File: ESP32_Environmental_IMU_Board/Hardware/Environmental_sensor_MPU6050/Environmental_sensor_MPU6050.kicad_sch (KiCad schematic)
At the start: 55 parts, among them J1 Conn_01x04_Pin, J2 Conn_01x04_Pin, J3 USB_C_Receptacle_USB2.0_16P, J4 Micro_SD_Card, SW1 SW_Push, SW2 SW_Push, U2 AP2112K-3.3, U3 USBLC6-2P6, U4 ESP32-S3-WROOM-1, U5 BME280, U6 DS3231M

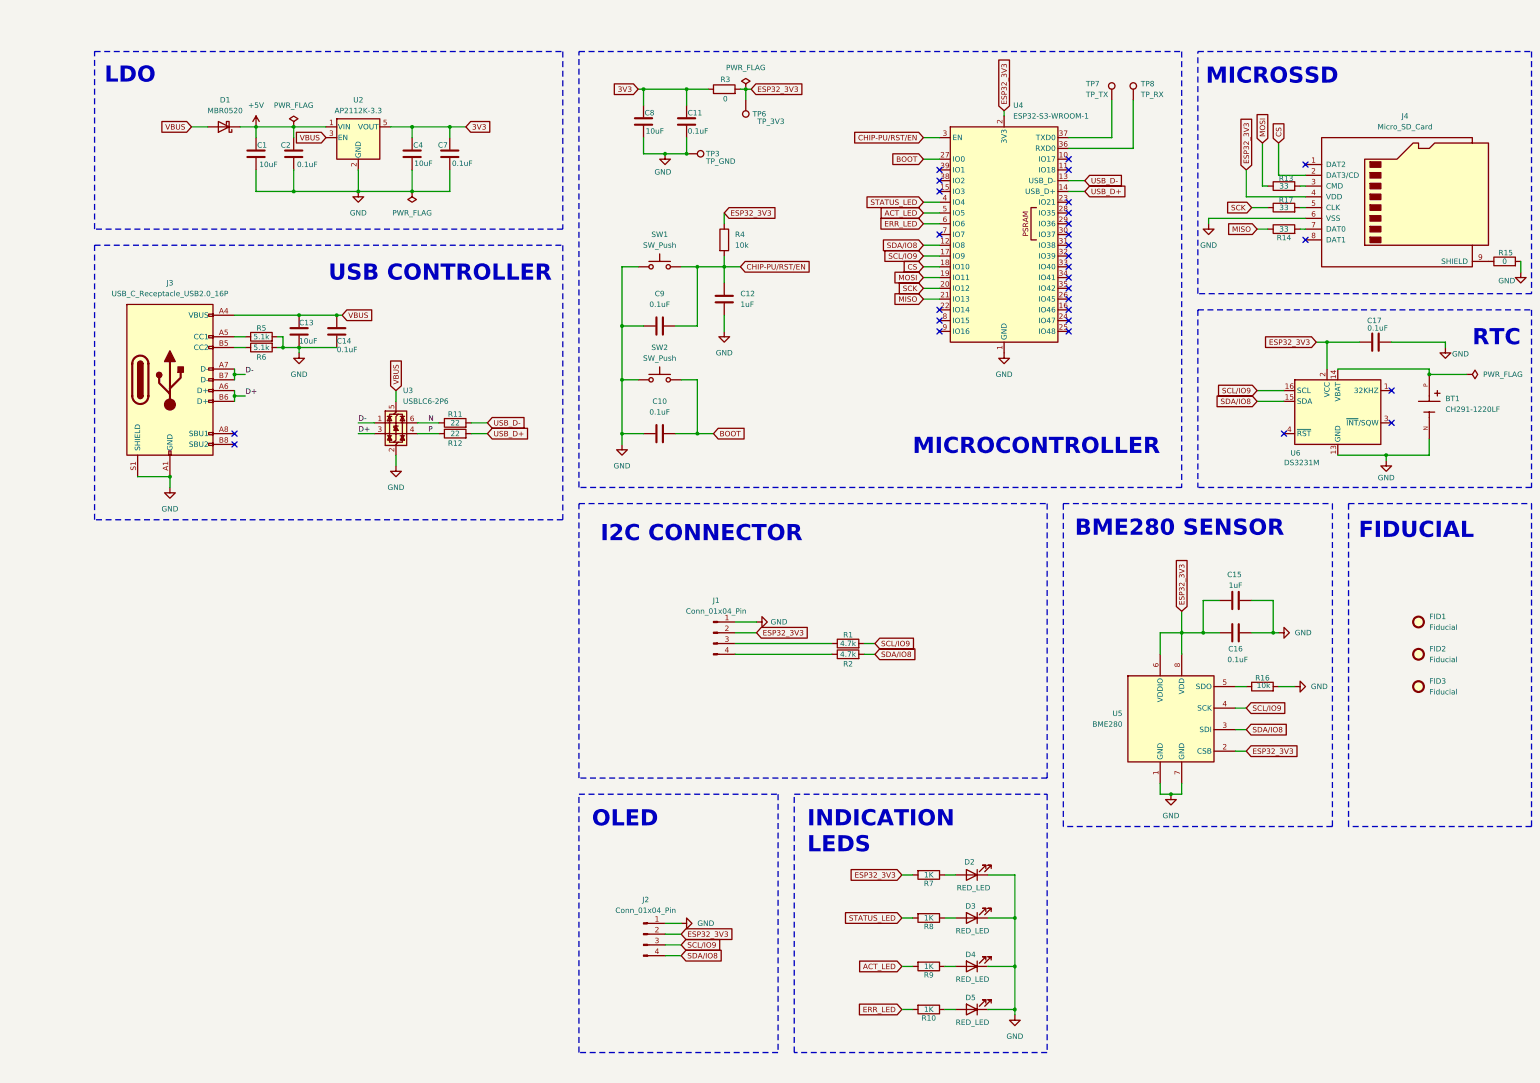
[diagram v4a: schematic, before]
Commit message: Charging moduke and buck converter added
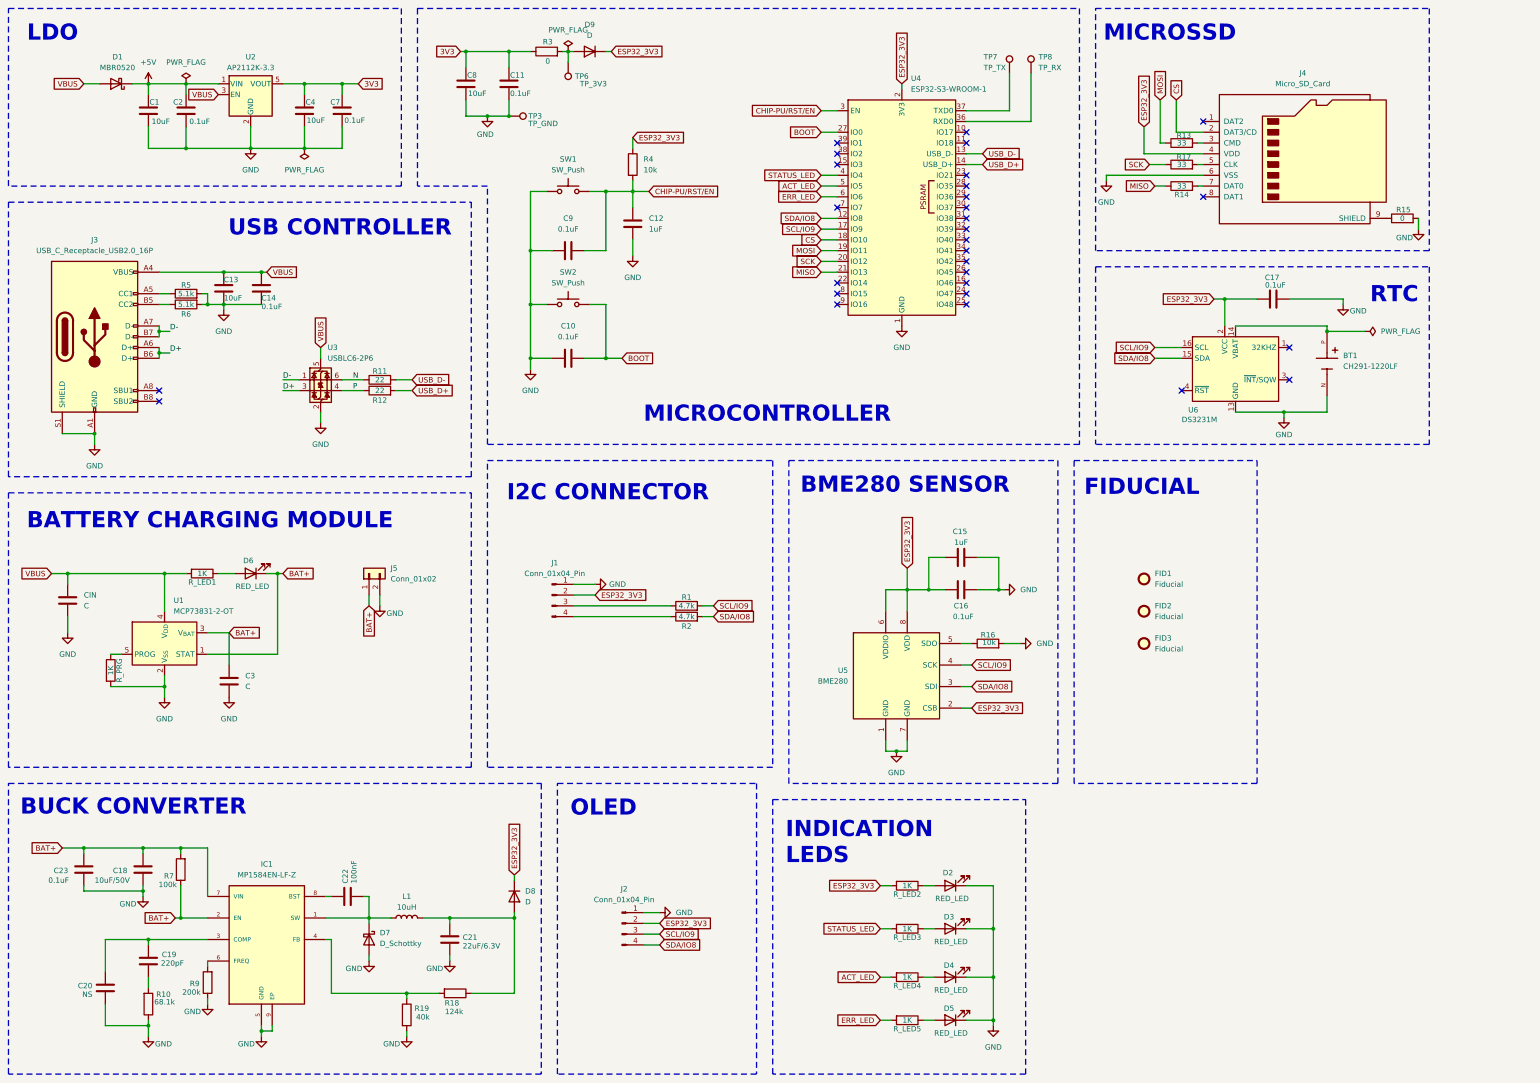
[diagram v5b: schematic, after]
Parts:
- added C18: 10uF/50V, Capacitor_SMD:C_0805_2012Metric, symbol Device:C
- added C19: 220pF, Capacitor_SMD:C_0805_2012Metric, symbol Device:C
- added C20: NS, Capacitor_SMD:C_0805_2012Metric, symbol Device:C
- added C21: 22uF/6.3V, Capacitor_SMD:C_0805_2012Metric, symbol Device:C
- added C22: 100nF, Capacitor_SMD:C_0805_2012Metric, symbol Device:C
- added C23: 0.1uF, Capacitor_SMD:C_0805_2012Metric, symbol Device:C
- added C3, CIN: C, symbol Device:C
- added D6: RED_LED, LED_SMD:LED_0201_0603Metric, symbol Device:LED
- added D7: D_Schottky, symbol Device:D_Schottky
- added D8, D9: D, symbol Device:D
- added IC1: MP1584EN-LF-Z, MP1584EN-LF-Z:SOIC127P600X170-9N, symbol MP1584EN-LF-Z:MP1584EN-LF-Z
- added J5: Conn_01x02, symbol Connector_Generic:Conn_01x02
- added L1: 10uH, symbol Device:L
- added R10: 68.1k, Resistor_SMD:R_0603_1608Metric, symbol Device:R
- added R18: 124k, Resistor_SMD:R_0603_1608Metric, symbol Device:R
- added R19: 40k, Resistor_SMD:R_0603_1608Metric, symbol Device:R
- added R7: 100k, Resistor_SMD:R_0603_1608Metric, symbol Device:R
- added R9: 200k, Resistor_SMD:R_0603_1608Metric, symbol Device:R
- added R_LED1, R_PRG: 1K, Resistor_SMD:R_0603_1608Metric, symbol Device:R
- added U1: MCP73831-2-OT, Package_TO_SOT_SMD:SOT-23-5, symbol Battery_Management:MCP73831-2-OT
- renumbered R7 to R_LED2, R8 to R_LED3, R9 to R_LED4, R10 to R_LED5
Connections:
- net ESP32_3V3: now also D8.1 (K), D9.1 (K); no longer R3.2, TP6.1
- net GND: now also C18.2, C20.2, C21.2, C23.2, C3.2, CIN.1, D7.2 (A), IC1.5 (GND), IC1.9 (EP), J5.2 (Pin_2), R10.1, R19.2, R9.1, R_PRG.2, U1.2 (V_{SS})
- net VBUS: now also CIN.2, R_LED1.2, U1.4 (V_{DD})
- new net: C22.2, D7.1 (K), IC1.1 (SW), L1.1
- new net: C19.1, C20.1, IC1.3 (COMP)
- new net: IC1.4 (FB), R18.2, R19.1
- new net: IC1.6 (FREQ), R9.2
- new net: C22.1, IC1.8 (BST)
- new net: C21.1, D8.2 (A), L1.2, R18.1
- new net: D9.2 (A), R3.2, TP6.1
- new net: C19.2, R10.2
- new net: D6.2 (A), R_LED1.1
- new net: R_PRG.1, U1.5 (PROG)
- new net BAT+: C18.1, C23.1, C3.1, D6.1 (K), IC1.2 (EN), IC1.7 (VIN), J5.1 (Pin_1), R7.1, R7.2, U1.1 (STAT), U1.3 (V_{BAT})
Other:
- note added: "BATTERY CHARGING MODULE"
- note added: "BUCK CONVERTER"
- moved on the sheet: BT1, C1, C10, C11, C12, C13, C14, C15, C16, C17, C2, C4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

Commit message: Sensor Architecture improvised in the Schematics
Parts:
- removed R1, R2: 4.7k, Resistor_SMD:R_0603_1608Metric, symbol Device:R
- added C22, C23: 100nF, Capacitor_SMD:C_0805_2012Metric, symbol Device:C
- added C24: 1uF, Capacitor_SMD:C_0603_1608Metric, symbol Device:C
- added C25: 0.1uF, Capacitor_SMD:C_0603_1608Metric, symbol Device:C
- added R12, R13: 4.7k, Resistor_SMD:R_0603_1608Metric, symbol Device:R
- added U10: MLX90614ESF-BAA-000-TU, MLX90614ESF-BAA-000-TU:TO254P942H425-4, symbol MLX90614ESF-BAA-000-TU:MLX90614ESF-BAA-000-TU
- added U6: SCD40-D-R2, Sensor:Sensirion_SCD4x-1EP_10.1x10.1mm_P1.25mm_EP4.8x4.8mm, symbol Sensor_Gas:SCD40-D-R2
- added U8: ENS160-BGLM, ENS160-BGLM:XDCR_ENS160-BGLM, symbol ENS160-BGLM:ENS160-BGLM
- added U9: OPT3001IDNPRQ1, OPT3001IDNPRQ1:SON65P200X200X65-7N, symbol OPT3001IDNPRQ1:OPT3001IDNPRQ1
- renumbered C23 to C1, C4 to C10, C7 to C11, C22 to C12, C21 to C13, C8 to C14, C11 to C15, C9 to C16, C10 to C17, C12 to C18, C15 to C19, C20 to C2, C16 to C20, C17 to C21, C18 to C3, C1 to C4, C19 to C5, C2 to C6, C13 to C7, C3 to C8, C14 to C9, CIN to CIN1, D6 to D2, D7 to D3, D8 to D4, D9 to D5, D2 to D6, D3 to D7, D4 to D8, D5 to D9, J3 to J1, J5 to J2, J2 to J3, J1 to J4, J4 to J5, R10 to R1, R3 to R10, R4 to R11, R16 to R14, R13 to R15, R17 to R16, R14 to R17, R15 to R18, R7 to R2, R5 to R3, R6 to R4, R9 to R5, R11 to R6, R12 to R7, R19 to R8, R18 to R9, R_PRG to R_PRG1, TP3 to TP1, TP6 to TP2, TP7 to TP3, TP8 to TP4, U5 to U4, U4 to U5, U6 to U7
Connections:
- net BAT+: no longer D2.1 (K), U1.1 (STAT)
- net ESP32_3V3: now also C22.1, C23.1, C24.1, C25.1, U10.3 (VDD), U6.19 (VDD), U6.7 (VDD), U8.4 (VDD), U8.5 (VDDIO), U8.7 (~{CS}), U9.1 (VDD)
- net GND: now also C22.2, C23.2, C24.2, C25.2, U10.4 (VSS), U6.20 (GND), U6.21 (GND), U6.6 (GND), U8.3 (MISO/ADDR), U8.8 (VSS), U8.9 (VSS), U9.2 (ADDR), U9.3 (GND), U9.7 (EXP)
- net SCL/IO9: now also J4.3 (Pin_3), R13.1, U10.1 (SCL/VZ), U6.9 (SCL), U8.2 (SCLK/SCL), U9.4 (SCL); no longer U5.17 (IO9)
- net SDA/IO8: now also J4.4 (Pin_4), R12.1, U10.2 (SDA/PWM), U6.10 (SDA), U8.1 (MOSI/SDA), U9.6 (SDA); no longer U5.12 (IO8)
- new net: R12.2, U5.12 (IO8)
- new net: R13.2, U5.17 (IO9)
- new net: D2.1 (K), U1.1 (STAT)
- no-connect marks 29 -> 31
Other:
- note added: "ENS160-MULTI GAS SENSOR"
- note added: "IR TEMP SENSOR"
- note added: "OLED DISPLAY"
- note added: "OPT001 AMBIENT LI8 SENSOR"
- note added: "SCD40 CO2 SENSOR"
- note removed: "OLED"
- moved on the sheet: BT1, C1, C10, C11, C12, C13, C14, C15, C16, C17, C18, C19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

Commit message: Footprints assigned
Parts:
- C8: value C -> 4.7uF; footprint (none) -> Capacitor_SMD:C_0805_2012Metric
- CIN1: value C -> 10uF; footprint (none) -> Capacitor_SMD:C_0805_2012Metric
- D3: footprint (none) -> Diode_SMD:D_SMA
- D4, D5: footprint (none) -> Diode_SMD:D_SOD-123F
- J2: footprint (none) -> Connector_JST:JST_PH_B2B-PH-K_1x02_P2.00mm_Vertical
- L1: footprint (none) -> Inductor_SMD:L_6.3x6.3_H3
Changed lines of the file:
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@@
 			)
 		)
-		(property "Value" "C"
+		(property "Value" "4.7uF"
 			(at 69.85 185.4199 0)
 			(show_name no)
@@
 			)
 		)
-		(property "Footprint" ""
+		(property "Footprint" "Capacitor_SMD:C_0805_2012Metric"
 			(at 67.0052 187.96 0)
 			(hide yes)
@@
 		(dnp no)
 		(fields_autoplaced yes)
-		(property "Reference" "#FLG04"
+		(property "Reference" "#FLG05"
 			(at 328.295 95.25 0)
 			(hide yes)
@@
 			(project "Environmental_sensor_MPU6050"
 				(path "/90ab1963-33c1-4a07-bcd3-34d44fb1eedd"
-					(reference "#FLG04")
+					(reference "#FLG05")
 					(unit 1)
 				)
@@
 			)
 		)
-		(property "Footprint" ""
+		(property "Footprint" "Diode_SMD:D_SOD-123F"
 			(at 133.35 228.6 0)
 			(hide yes)
@@
 			)
 		)
-		(property "Footprint" ""
+		(property "Footprint" "Diode_SMD:D_SMA"
 			(at 99.06 238.76 0)
 			(hide yes)
@@
 			)
 		)
-		(property "Footprint" ""
+		(property "Footprint" "Connector_JST:JST_PH_B2B-PH-K_1x02_P2.00mm_Vertical"
 			(at 99.06 152.4 0)
 			(hide yes)
@@
 		(dnp no)
 		(fields_autoplaced yes)
-		(property "Reference" "#FLG02"
+		(property "Reference" "#FLG03"
 			(at 83.82 53.975 0)
 			(hide yes)
@@
 			(project "Environmental_sensor_MPU6050"
 				(path "/90ab1963-33c1-4a07-bcd3-34d44fb1eedd"
-					(reference "#FLG02")
+					(reference "#FLG03")
 					(unit 1)
 				)
@@
 		(dnp no)
 		(fields_autoplaced yes)
-		(property "Reference" "#FLG06"
+		(property "Reference" "#FLG04"
 			(at 158.75 27.305 0)
 			(hide yes)
@@
 			(project "Environmental_sensor_MPU6050"
 				(path "/90ab1963-33c1-4a07-bcd3-34d44fb1eedd"
-					(reference "#FLG06")
+					(reference "#FLG04")
 					(unit 1)
 				)
@@
 			)
 		)
-		(property "Value" "C"
+		(property "Value" "10uF"
 			(at 31.75 160.0199 0)
 			(show_name no)
@@
 			)
 		)
-		(property "Footprint" ""
+		(property "Footprint" "Capacitor_SMD:C_0805_2012Metric"
 			(at 26.9748 154.94 0)
 			(hide yes)
@@
 			)
 		)
-		(property "Footprint" ""
+		(property "Footprint" "Diode_SMD:D_SOD-123F"
 			(at 151.13 29.21 0)
 			(hide yes)
@@
 			)
 		)
-		(property "Footprint" ""
+		(property "Footprint" "Inductor_SMD:L_6.3x6.3_H3"
 			(at 107.95 233.68 0)
 			(hide yes)
@@
 		(dnp no)
 		(fields_autoplaced yes)
-		(property "Reference" "#FLG05"
+		(property "Reference" "#FLG01"
 			(at 27.94 150.495 0)
 			(hide yes)
@@
 			(project "Environmental_sensor_MPU6050"
 				(path "/90ab1963-33c1-4a07-bcd3-34d44fb1eedd"
-					(reference "#FLG05")
+					(reference "#FLG01")
 					(unit 1)
 				)
@@
 		(dnp no)
 		(property "Reference" "R_PRG1"
-			(at 40.132 175.26 90)
+			(at 35.306 175.26 90)
 			(show_name no)
 			(do_not_autoplace no)
@@
 		(dnp no)
 		(fields_autoplaced yes)
-		(property "Reference" "#FLG01"
+		(property "Reference" "#FLG02"
 			(at 55.88 34.925 0)
 			(hide yes)
@@
 			(project "Environmental_sensor_MPU6050"
 				(path "/90ab1963-33c1-4a07-bcd3-34d44fb1eedd"
-					(reference "#FLG01")
+					(reference "#FLG02")
 					(unit 1)
 				)

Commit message: Battery footprint changed
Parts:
- J2: footprint Connector_JST:JST_PH_B2B-PH-K_1x02_P2.00mm_Vertical -> Connector_JST:JST_PH_S2B-PH-K_1x02_P2.00mm_Horizontal
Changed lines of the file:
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@@
 			)
 		)
-		(property "Footprint" "Connector_JST:JST_PH_B2B-PH-K_1x02_P2.00mm_Vertical"
+		(property "Footprint" "Connector_JST:JST_PH_S2B-PH-K_1x02_P2.00mm_Horizontal"
 			(at 99.06 152.4 0)
 			(hide yes)
